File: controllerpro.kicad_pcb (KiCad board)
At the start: 2 copper layers, 92.7 x 50.8 mm, 19 parts, among them P0 Conn_01x08_Male, P2 Conn_01x08_Male, U1 Teensy3.2

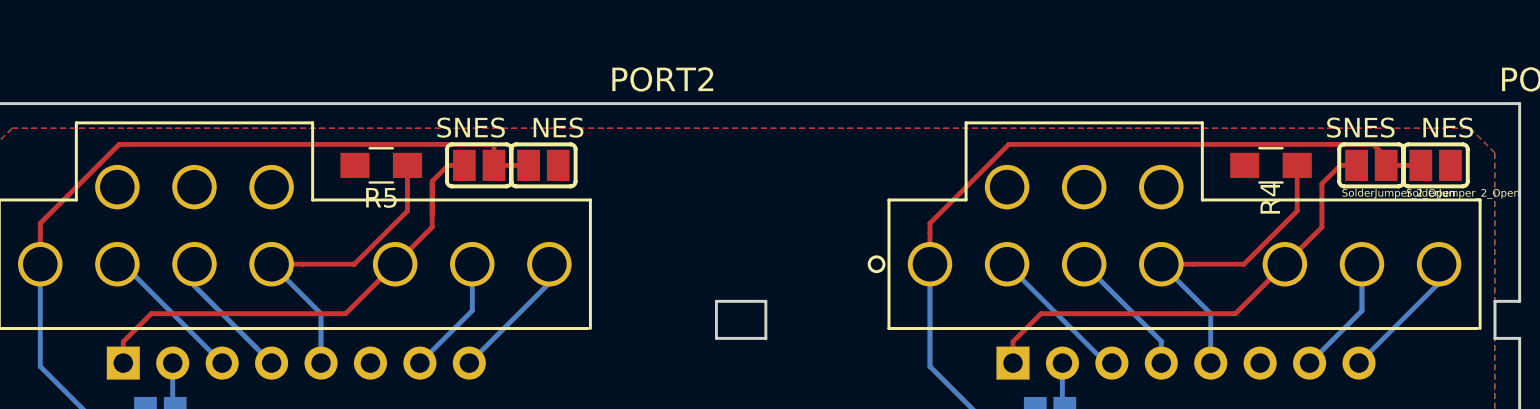
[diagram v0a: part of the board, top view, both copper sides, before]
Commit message: Make controller pin holes smaller
Finally found a datasheet that recommends a reasonable size
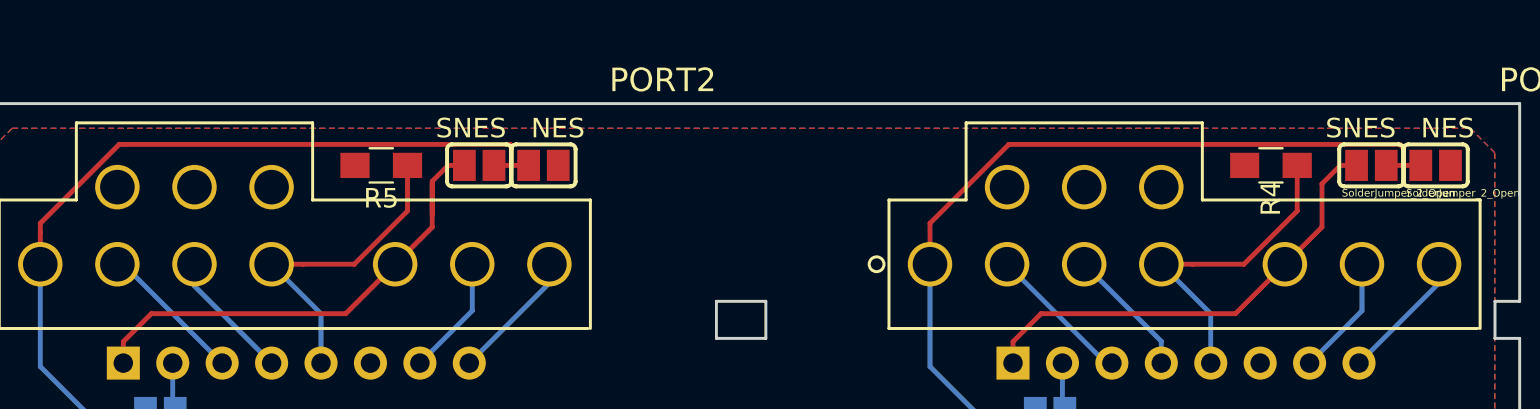
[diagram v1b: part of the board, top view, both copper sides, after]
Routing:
- net Net-(JP2-Pad1): track 45.5 -> 46.6 mm
- net Net-(JP5-Pad1): track 45.5 -> 46.4 mm
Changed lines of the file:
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@@
     (thickness 1.6)
     (drawings 88)
-    (tracks 216)
+    (tracks 218)
     (zones 0)
     (modules 19)
@@
       (effects (font (size 1 1) (thickness 0.15)))
     )
-    (fp_text user %R (at 0 0 180) (layer B.Fab)
-      (effects (font (size 0.5 0.5) (thickness 0.075)) (justify mirror))
+    (fp_text user %R (at 0 0 180) (layer F.Fab)
+      (effects (font (size 0.5 0.5) (thickness 0.075)))
     )
     (fp_line (start -1 0.62) (end -1 -0.62) (layer F.Fab) (width 0.1))
@@
   (segment (start 179.578 127.635) (end 178.7438 127.635) (width 0.25) (layer Top) (net 36))
   (segment (start 178.7438 127.635) (end 177.8 128.5788) (width 0.25) (layer Top) (net 36))
-  (segment (start 135.255 127.635) (end 137.033 127.635) (width 0.25) (layer Top) (net 48) (status 1000000))
-  (segment (start 135.255 127.635) (end 135.255 126.5849) (width 0.25) (layer Top) (net 48))
+  (segment (start 136.144 127.635) (end 136.144 126.619) (width 0.25) (layer Top) (net 48))
+  (segment (start 136.082499 126.557499) (end 136.144 126.619) (width 0.25) (layer Top) (net 48))
+  (segment (start 135.001 126.557499) (end 115.993107 126.557499) (width 0.25) (layer Top) (net 48))
+  (segment (start 135.001 126.557499) (end 136.082499 126.557499) (width 0.25) (layer Top) (net 48))
+  (segment (start 135.255 127.635) (end 136.144 127.635) (width 0.25) (layer Top) (net 48))
+  (segment (start 136.144 127.635) (end 137.033 127.635) (width 0.25) (layer Top) (net 48))
   (segment (start 111.9378 131.098554) (end 111.9378 132.715) (width 0.25) (layer Top) (net 48))
-  (segment (start 135.227599 126.557499) (end 115.993107 126.557499) (width 0.25) (layer Top) (net 48))
   (segment (start 115.993107 126.557499) (end 111.9378 130.612806) (width 0.25) (layer Top) (net 48))
   (segment (start 111.9378 130.612806) (end 111.9378 131.098554) (width 0.25) (layer Top) (net 48))
-  (segment (start 135.255 126.5849) (end 135.227599 126.557499) (width 0.25) (layer Top) (net 48))
   (segment (start 111.9378 132.715) (end 111.9378 137.9728) (width 0.25) (layer Bottom) (net 48))
   (segment (start 111.9378 137.9728) (end 114.3 140.335) (width 0.25) (layer Bottom) (net 48))
@@
   (segment (start 105.283 95.885) (end 105.283 96.647) (width 1) (layer Bottom) (net 47))
   (segment (start 105.283 96.647) (end 104.14 97.79) (width 1) (layer Bottom) (net 47))
-  (segment (start 182.88 127.635) (end 181.102 127.635) (width 0.25) (layer Top) (net 49))
-  (segment (start 181.102 127.635) (end 181.102 127.2199) (width 0.25) (layer Top) (net 49))
-  (segment (start 181.102 127.2199) (end 180.467 126.5849) (width 0.25) (layer Top) (net 49))
-  (segment (start 161.713107 126.557499) (end 157.6578 130.612806) (width 0.25) (layer Top) (net 49))
-  (segment (start 157.6578 130.612806) (end 157.6578 131.098554) (width 0.25) (layer Top) (net 49))
-  (segment (start 180.467 126.5849) (end 180.439599 126.557499) (width 0.25) (layer Top) (net 49))
-  (segment (start 180.439599 126.557499) (end 161.713107 126.557499) (width 0.25) (layer Top) (net 49))
-  (segment (start 157.6578 131.098554) (end 157.6578 132.715) (width 0.25) (layer Top) (net 49))
+  (segment (start 157.6578 130.612806) (end 161.713107 126.557499) (width 0.25) (layer Top) (net 49))
+  (segment (start 157.6578 132.715) (end 157.6578 130.612806) (width 0.25) (layer Top) (net 49))
+  (segment (start 181.991 126.746) (end 181.991 127) (width 0.25) (layer Top) (net 49))
+  (segment (start 161.713107 126.557499) (end 181.802499 126.557499) (width 0.25) (layer Top) (net 49))
+  (segment (start 181.802499 126.557499) (end 181.991 126.746) (width 0.25) (layer Top) (net 49))
+  (segment (start 181.991 127.635) (end 181.991 127) (width 0.25) (layer Top) (net 49))
+  (segment (start 182.88 127.635) (end 181.991 127.635) (width 0.25) (layer Top) (net 49))
+  (segment (start 181.991 127.635) (end 181.102 127.635) (width 0.25) (layer Top) (net 49))
   (segment (start 163.068 140.335) (end 160.02 140.335) (width 0.25) (layer Bottom) (net 49))
   (segment (start 160.02 140.335) (end 157.6578 137.9728) (width 0.25) (layer Bottom) (net 49))

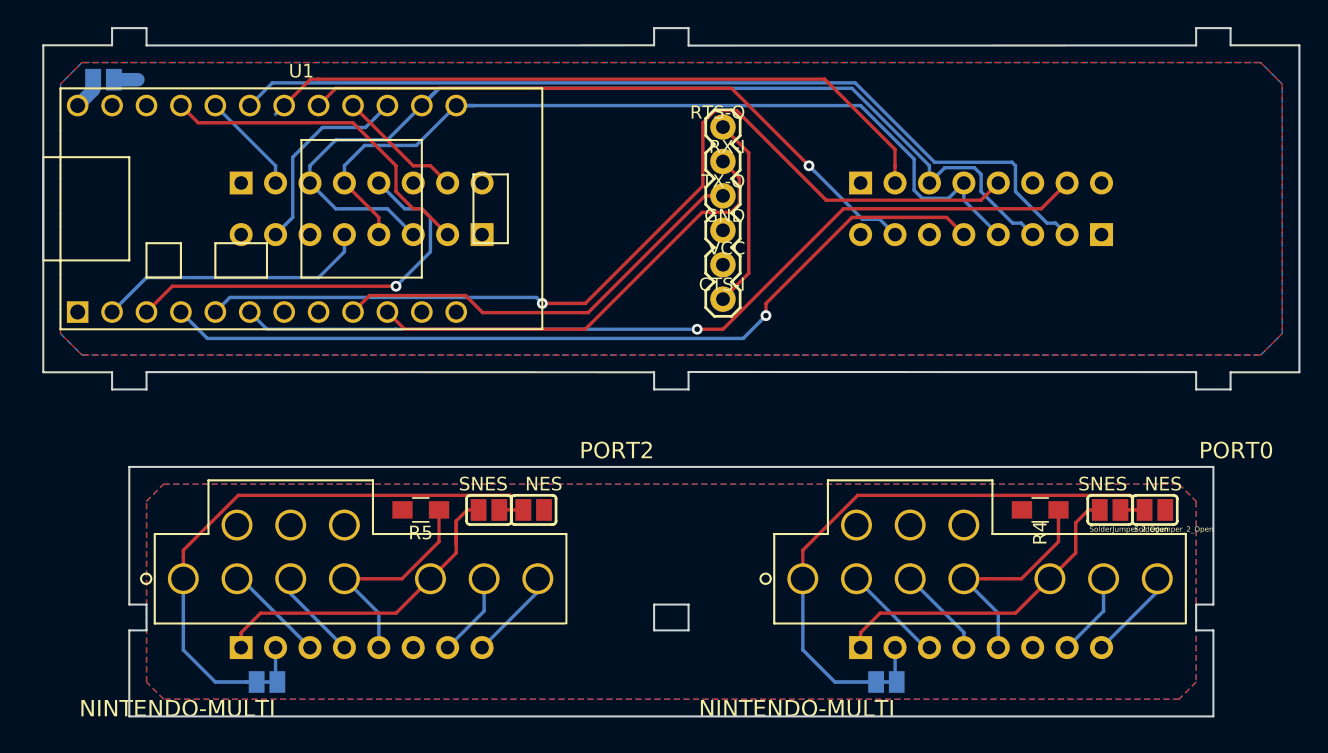
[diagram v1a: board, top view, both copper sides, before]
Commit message: Shrink top board considerably
So much empty space!
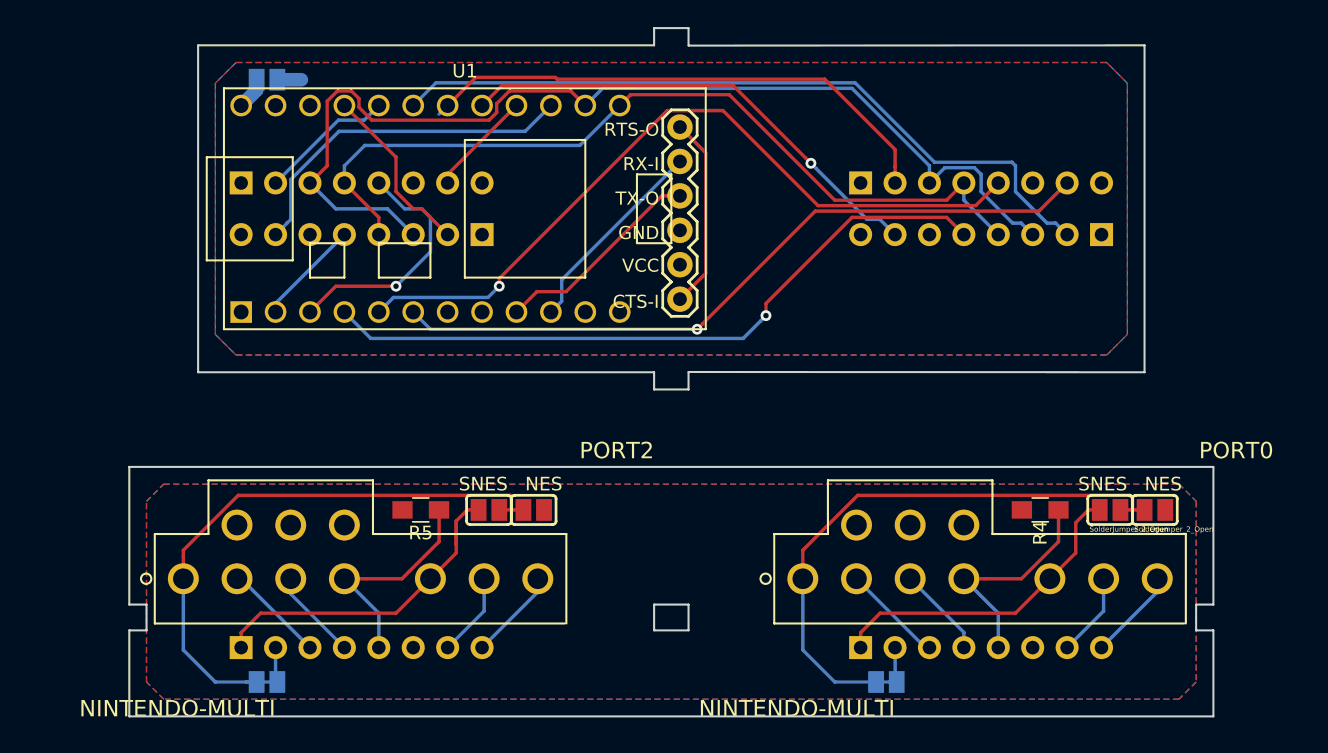
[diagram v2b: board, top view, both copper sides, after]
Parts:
- PORT2: footprint controllerpro:NINTENDO-MULTI -> NINTENDO-MULTI
- moved JP1 12.1 mm to (118.1, 95.9)
- moved U1 12.1 mm to (132.7, 105.4)
- moved U$1 3.17 mm to (148.6, 105.7)
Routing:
- net Net-(U$1-PadRX-I): track 34.0 -> 15.1 mm
- net Net-(U$1-PadTX-0): track 31.9 -> 15.6 mm
- net 5VDATA1: track 70.3 -> 55.8 mm
- net 5VDATA2: track 20.3 -> 7.82 mm
- net S_OR_NES0: track 66.8 -> 54.7 mm
- net 5VDATA3: track 30.2 -> 18.1 mm
- net 5VDATA0: track 63.3 -> 51.3 mm
- net 3VDATA1: track 65.3 -> 53.3 mm
- net S_OR_NES1: track 51.4 -> 39.5 mm
- net 3VDATA0: track 47.5 -> 35.7 mm
- net S_OR_NES2: track 24.7 -> 13.1 mm
- net 3VDATA2: track 14.8 -> 26.0 mm
- net CLOCK: track 74.8 -> 78.6 mm
- net S_OR_NES3: track 7.56 -> 9.99 mm
- net 3VDATA3: track 9.35 -> 7.82 mm
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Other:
- board size 92.7 x 50.8 mm -> 80 x 50.8 mm

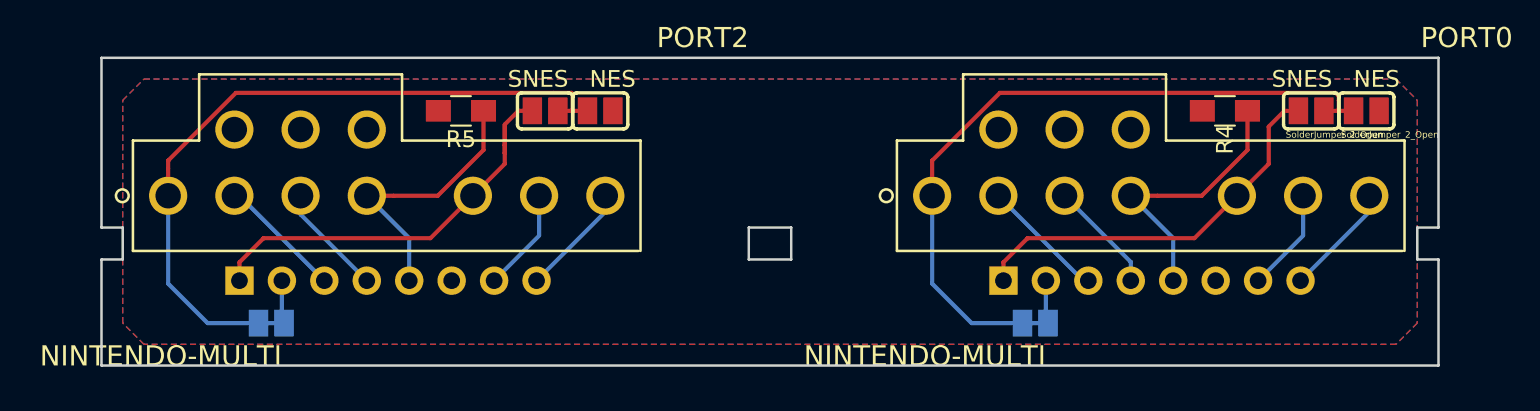
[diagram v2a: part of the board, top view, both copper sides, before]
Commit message: Make the bottom board smaller!
SMALLER SMALLER SMALLER
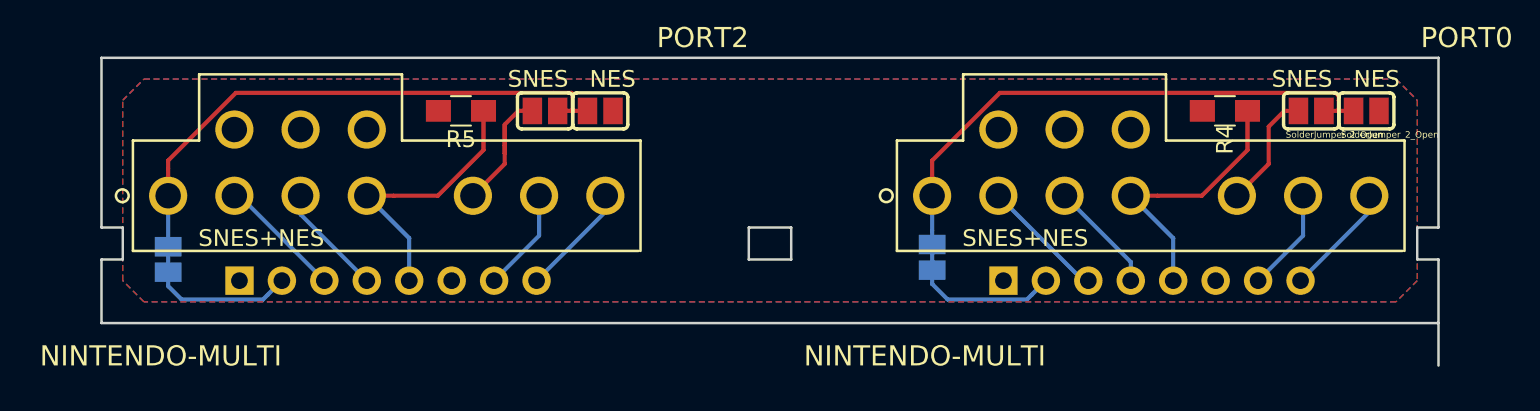
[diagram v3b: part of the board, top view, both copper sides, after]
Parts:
- moved JP2 7.32 mm to (157.7, 136.4), turned to 270 degrees
- moved JP5 7.25 mm to (111.9, 136.5), turned to 270 degrees
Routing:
- net VCCA: track 49.2 -> 15.8 mm
- net Net-(JP2-Pad1): track 46.6 -> 43.8 mm
- net Net-(JP5-Pad1): track 46.4 -> 43.8 mm
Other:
- outline, holes or cut-outs redrawn

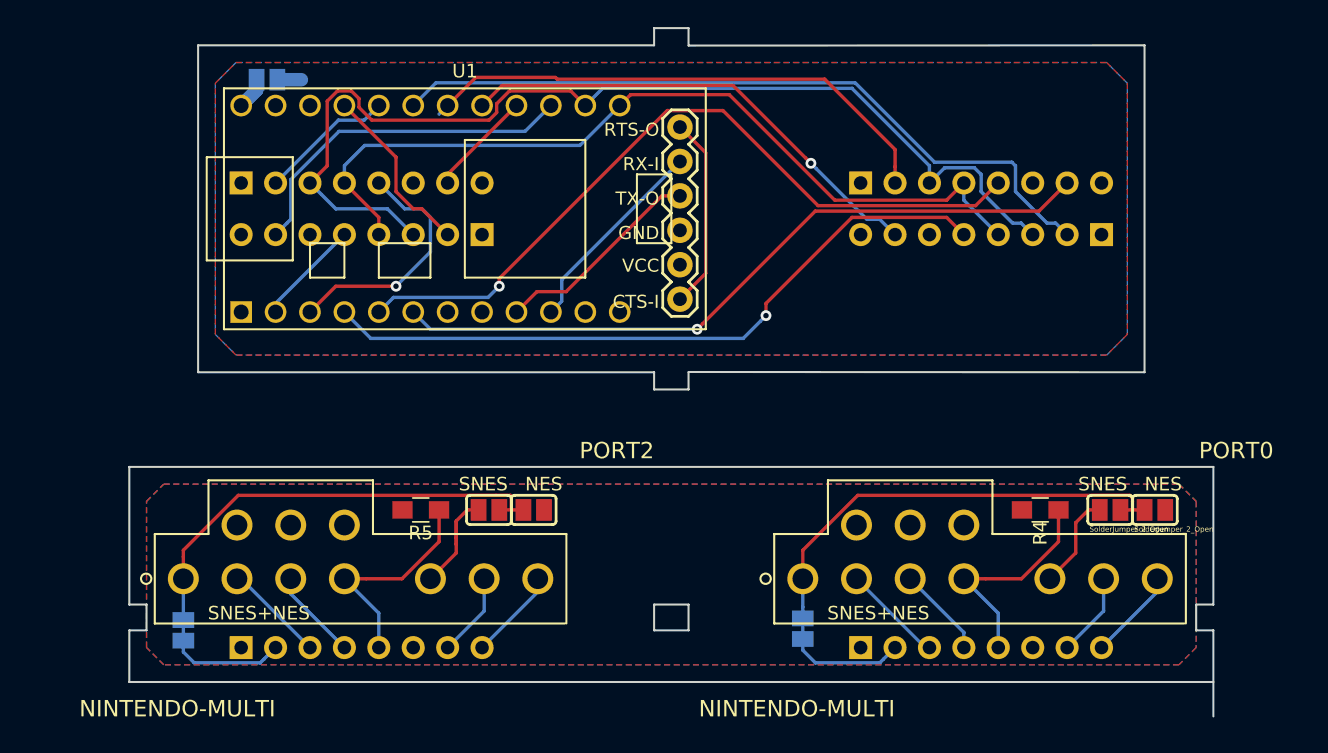
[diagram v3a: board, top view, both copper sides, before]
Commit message: Silkscreen!!
Logos! Labels!
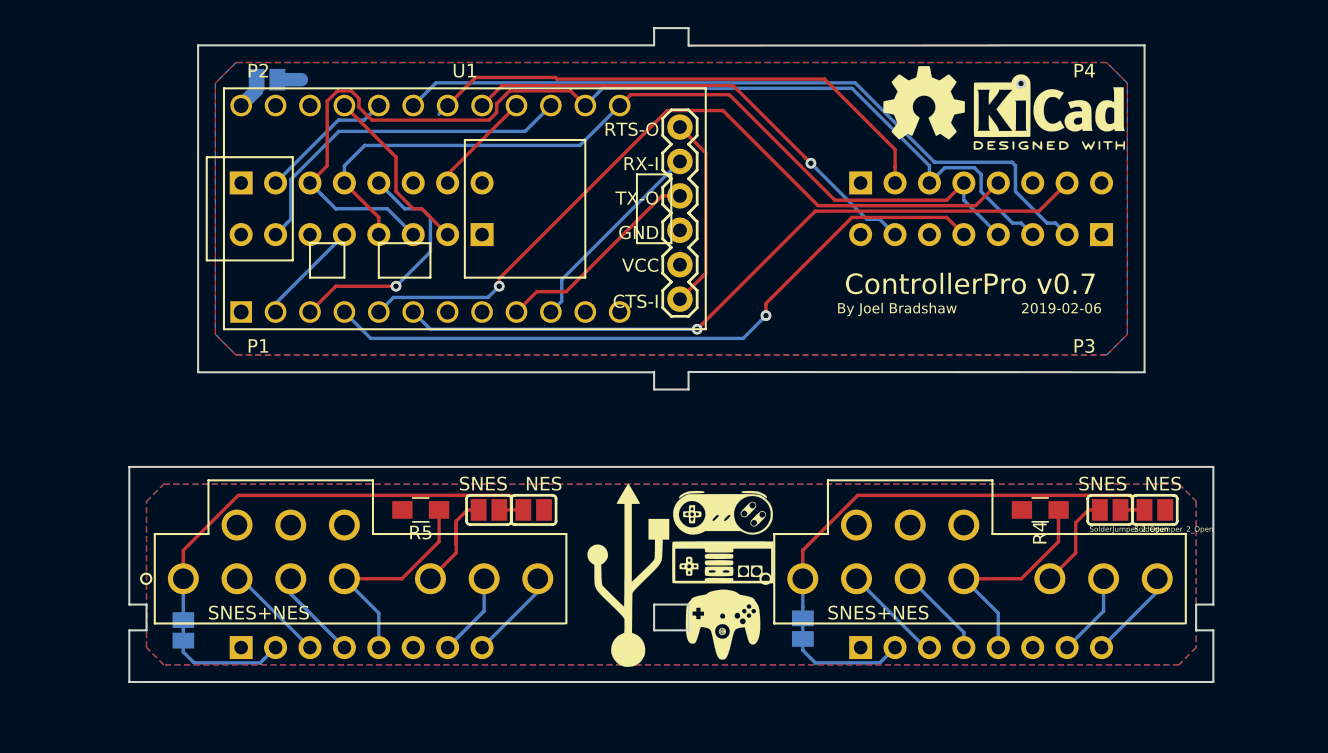
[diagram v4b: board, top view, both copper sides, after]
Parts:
- added G***: LOGO, logos:OSHlogo, F.Cu at (166.6, 97.7)
- added G***: LOGO, logos:square_logo, F.Cu at (148.6, 132.5)
- added G***: LOGO, logos:qrcode, B.Cu at (147.8, 132.3)
- added G***: LOGO, logos:designedwithkicad, F.Cu at (175.8, 98.3)
- added G***: LOGO, logos:sideways, B.Cu at (150.3, 107.7)
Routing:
- net GND: vias 0 -> 1
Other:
- board size 80 x 50.8 mm -> 80 x 48.3 mm
- board text added: "2019-02-06"
- board text added: "ControllerPro v0.7"
- board text added: "P1"
- board text added: "P2"
- board text added: "P3"
- board text added: "P4"

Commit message: Nudge bluetooth, refining silkscreen/labels
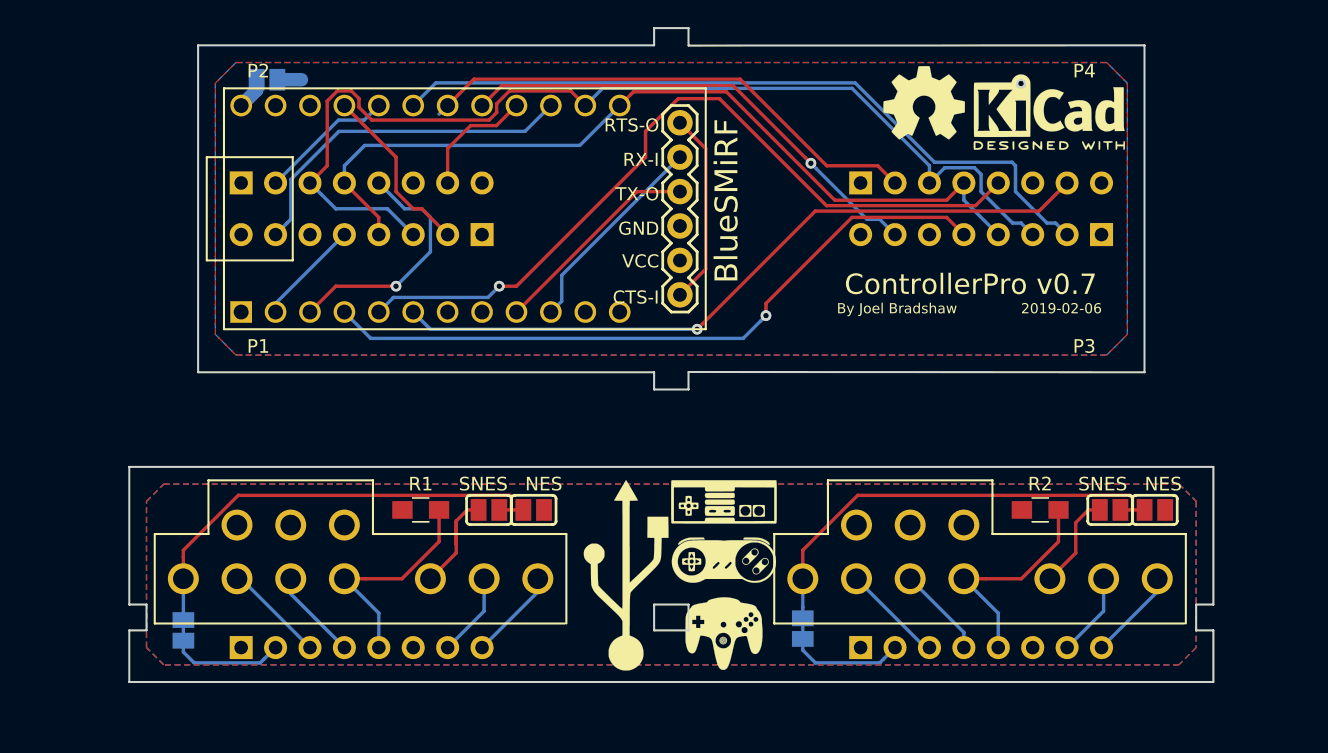
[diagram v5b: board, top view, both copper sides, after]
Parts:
- PORT2: footprint NINTENDO-MULTI -> controllerpro:NINTENDO-MULTI
- moved U$1 0.32 mm to (148.6, 105.4)
- renumbered R5 to R1, R4 to R2
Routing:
- net 3VDATA3: track 7.82 -> 9.57 mm
- net S_OR_NES1: track 39.5 -> 37.9 mm
- net 5VDATA1: track 55.8 -> 57.3 mm
